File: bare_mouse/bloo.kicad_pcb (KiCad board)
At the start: 2 copper layers, 100 x 105.9 mm, 103 parts, among them J1 Serial Debug Header, J10 Conn_01x06_Female, J2 SWD Header, J4 Conn_ARM_JTAG_SWD_10, J5 SWD Header, M1 M1_Conn_Alt, M2 M2_Conn_Alt, Q0 TEFT4300, Q1 TEFT4300, Q10 Q_NMOS_GSD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

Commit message: updating repo with Justin's pcb
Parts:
- moved C14 214.0 mm to (262.0, 223.9)
- moved C15 214.0 mm to (262.0, 227.3)
- moved C21 209.7 mm to (255.5, 227.3)
- moved C20 209.7 mm to (255.5, 223.9)
- moved R1 194.1 mm to (269.1, 219.4)
- moved R2 194.1 mm to (269.1, 222.7)
- moved R3 194.1 mm to (269.1, 226.0)
- moved R4 194.1 mm to (269.1, 229.3)
- moved C4 190.4 mm to (303.6, 130.6)
- moved C3 189.6 mm to (303.6, 125.5)
- moved C6 174.3 mm to (301.6, 156.0)
- moved C8 174.3 mm to (301.6, 158.5)
- moved FB3 174.3 mm to (301.6, 161.0)
- moved FB4 174.3 mm to (301.6, 163.5)
- moved C1 172.9 mm to (298.3, 87.0)
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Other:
- board text added: "BUTTON Parts"
- board text added: "BUTTON_2 Parts"
- board text added: "BUTTON_3 Parts"
- board text added: "Battery Mounts"
- board text added: "Bottom Pair of Power Supply"
- board text added: "Buzzer Parts"
- board text added: "Emitter Parts"
- board text added: "LED Blue Parts"
- board text added: "LED Green Parts"
- board text added: "LED Red Parts"
- board text added: "Power ORing Parts"
- board text added: "RST Parts"
- board text added: "Receiver Parts"
- board text added: "SWD Header Parts"
- board text added: "Skates"
- board text added: "Top Pair of Power Supply"
- board text added: "U2 L293D Parts"

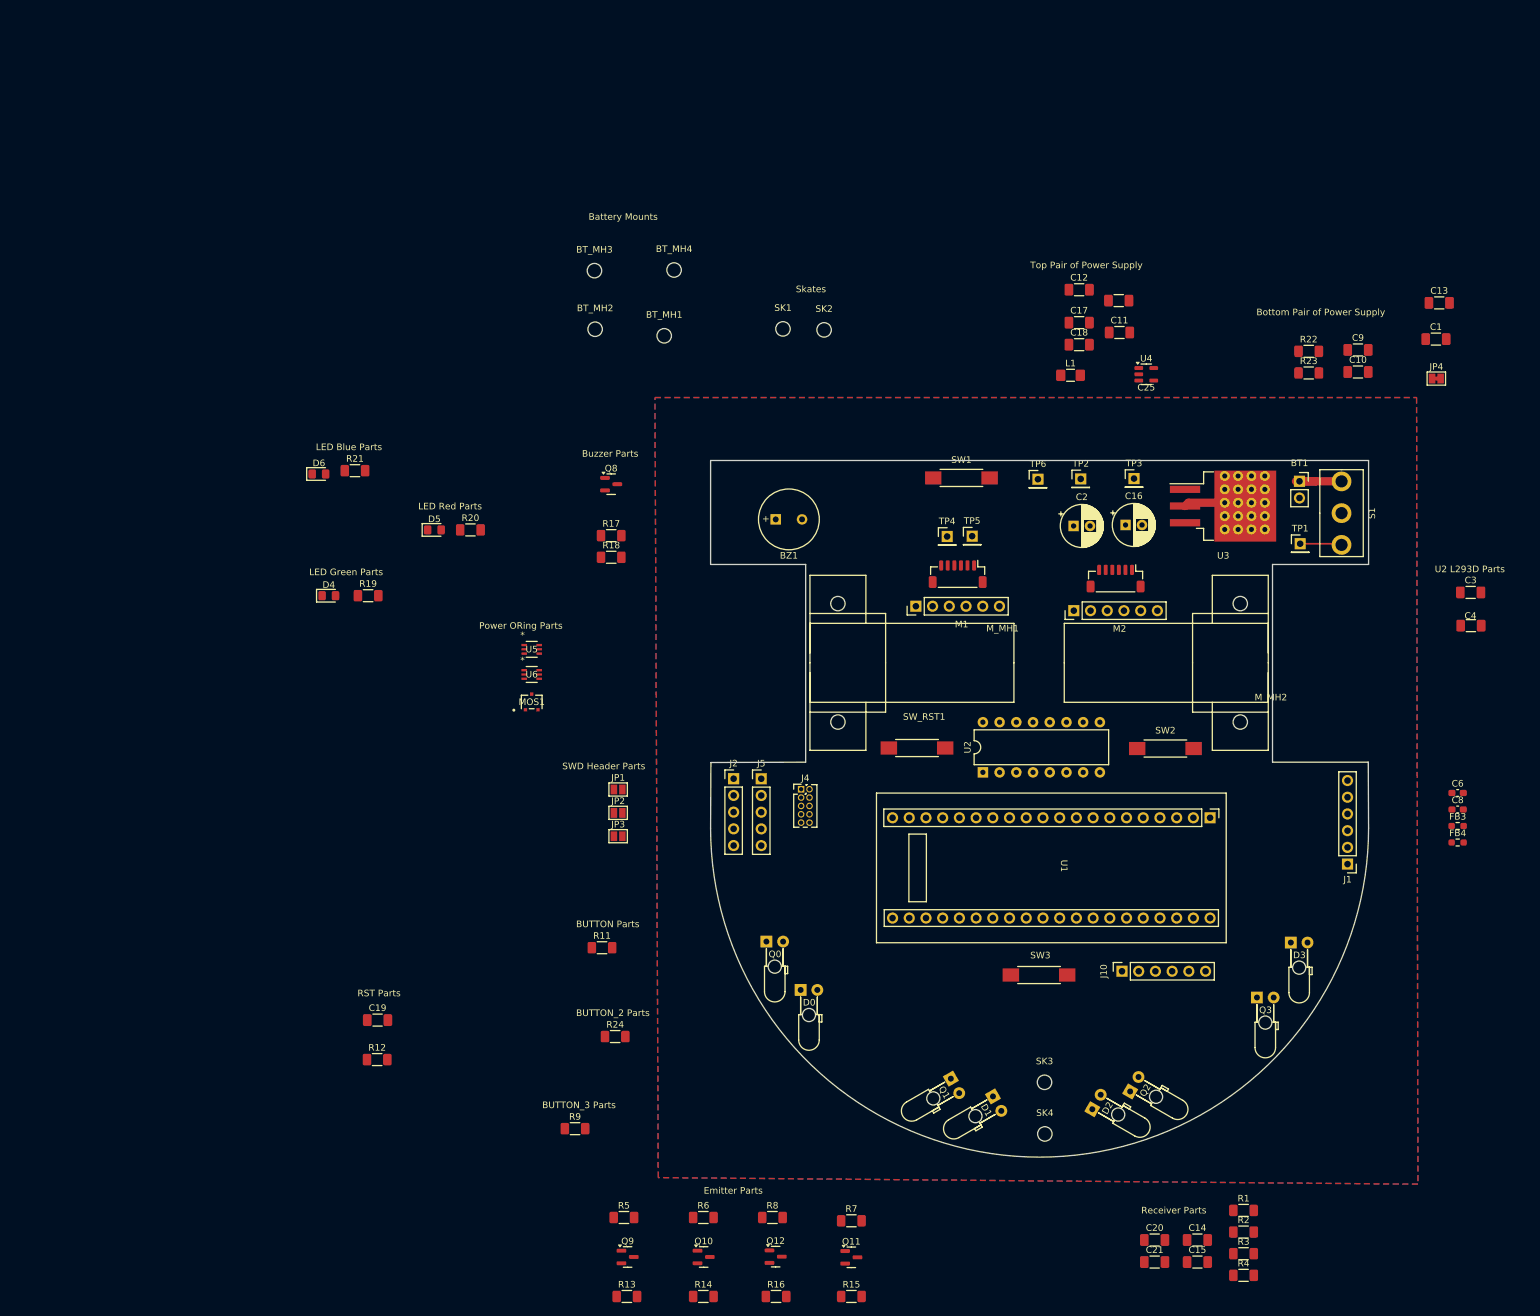
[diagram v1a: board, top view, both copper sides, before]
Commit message: placed components and attempted power traces
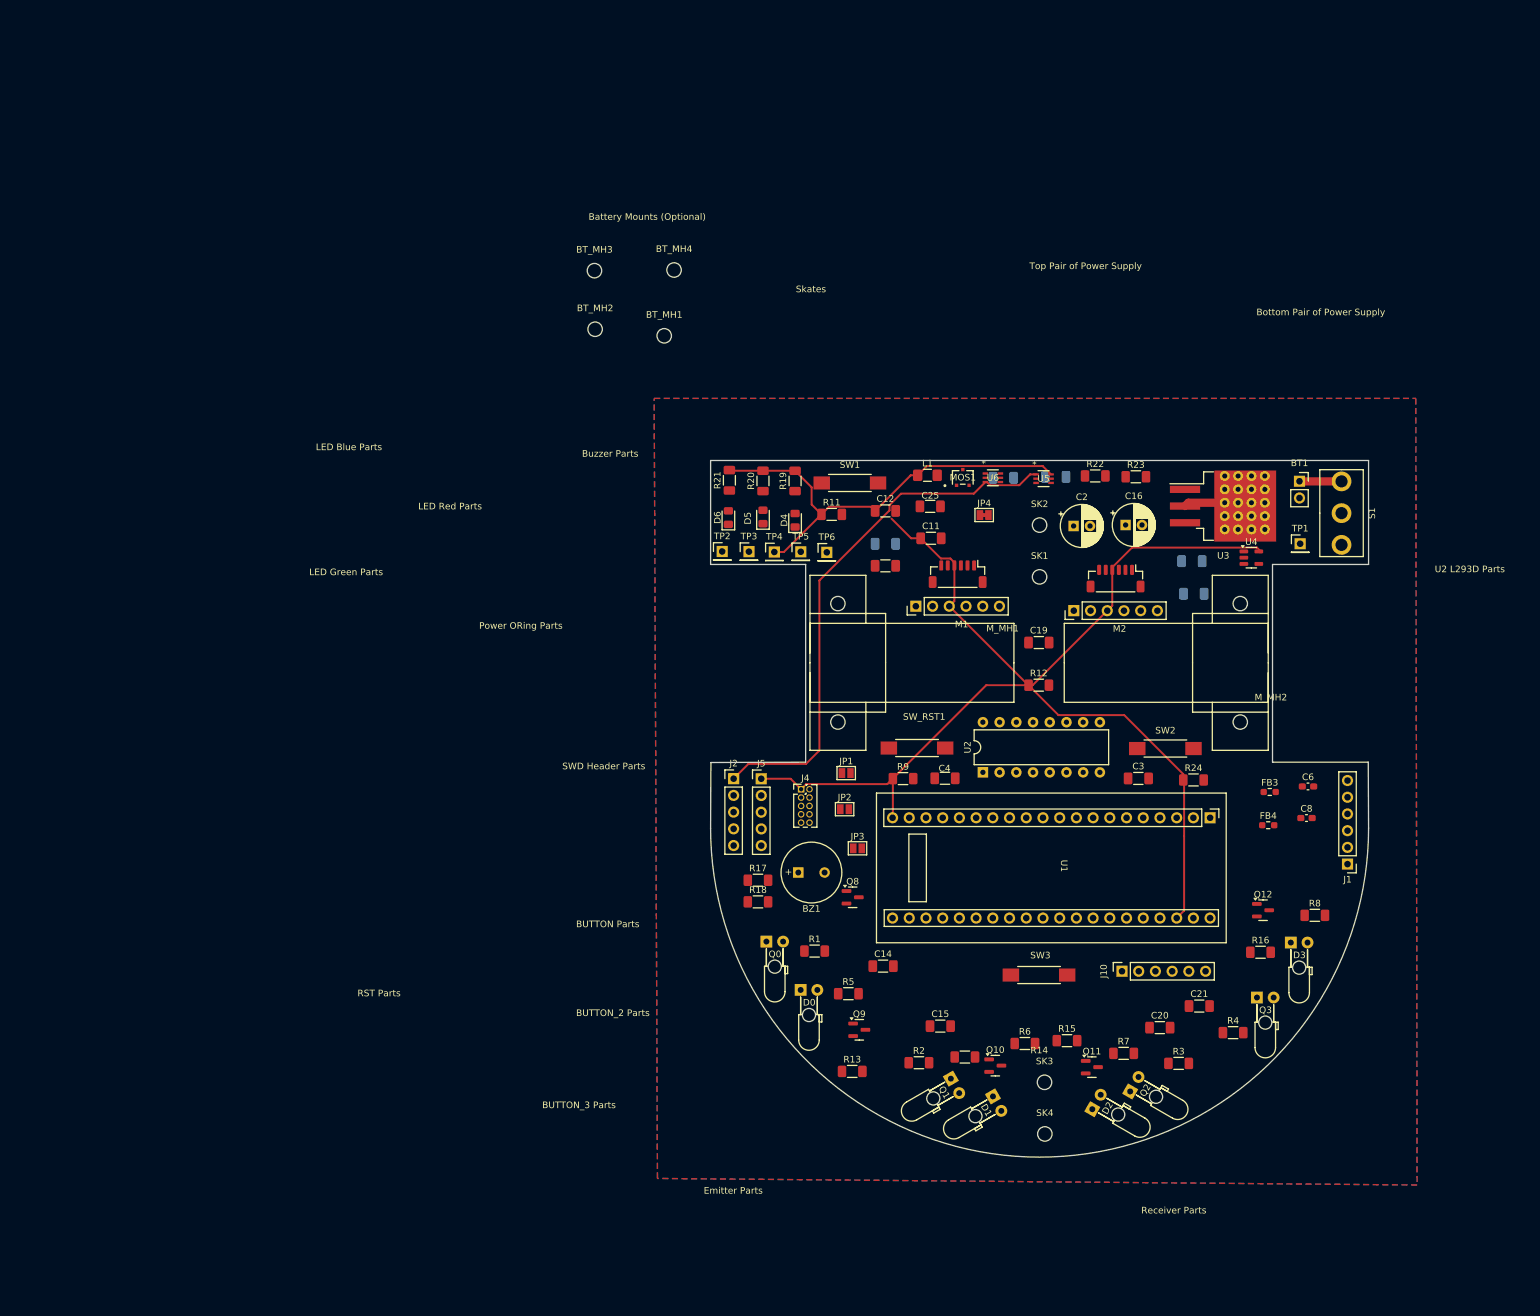
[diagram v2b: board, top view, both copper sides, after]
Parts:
- C1, C10, C13, C17, C9: moved to B.Cu
- moved C19 115.7 mm to (237.9, 133.1)
- moved R12 115.5 mm to (237.9, 139.6)
- moved R24 96.2 mm to (261.4, 154.0)
- moved R8 94.4 mm to (279.9, 174.6)
- moved Q12 90.9 mm to (272.0, 173.8)
- moved R16 90.3 mm to (271.6, 180.2)
- moved C4 83.2 mm to (223.7, 153.7)
- moved U5 82.0 mm to (238.7, 108.2)
- moved U6 76.2 mm to (230.9, 108.1)
- moved R1 76.2 mm to (203.9, 180.0)
- moved R11 74.5 mm to (206.5, 113.6)
- moved MOS1 73.9 mm to (226.4, 108.0)
- moved R9 72.9 mm to (217.3, 153.8)
- moved Q8 72.7 mm to (209.6, 171.8)
- moved D4 71.8 mm to (200.9, 114.5), turned to 90 degrees
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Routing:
- net +3V3: track 0.00 -> 256.6 mm
- net +3V3_NET: track 0.00 -> 81.1 mm
- net Net-(S1-Pad3): track 6.52 -> 0.40 mm
- net Net-(BT1-+): track 9.45 -> 6.42 mm
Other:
- board text added: "Battery Mounts (Optional)"
- board text removed: "Battery Mounts"
